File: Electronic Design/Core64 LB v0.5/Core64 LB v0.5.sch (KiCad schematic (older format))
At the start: 9 parts, among them J12 TEENSY Cur. Mon., J4 PRG, U2 Teensy3.2

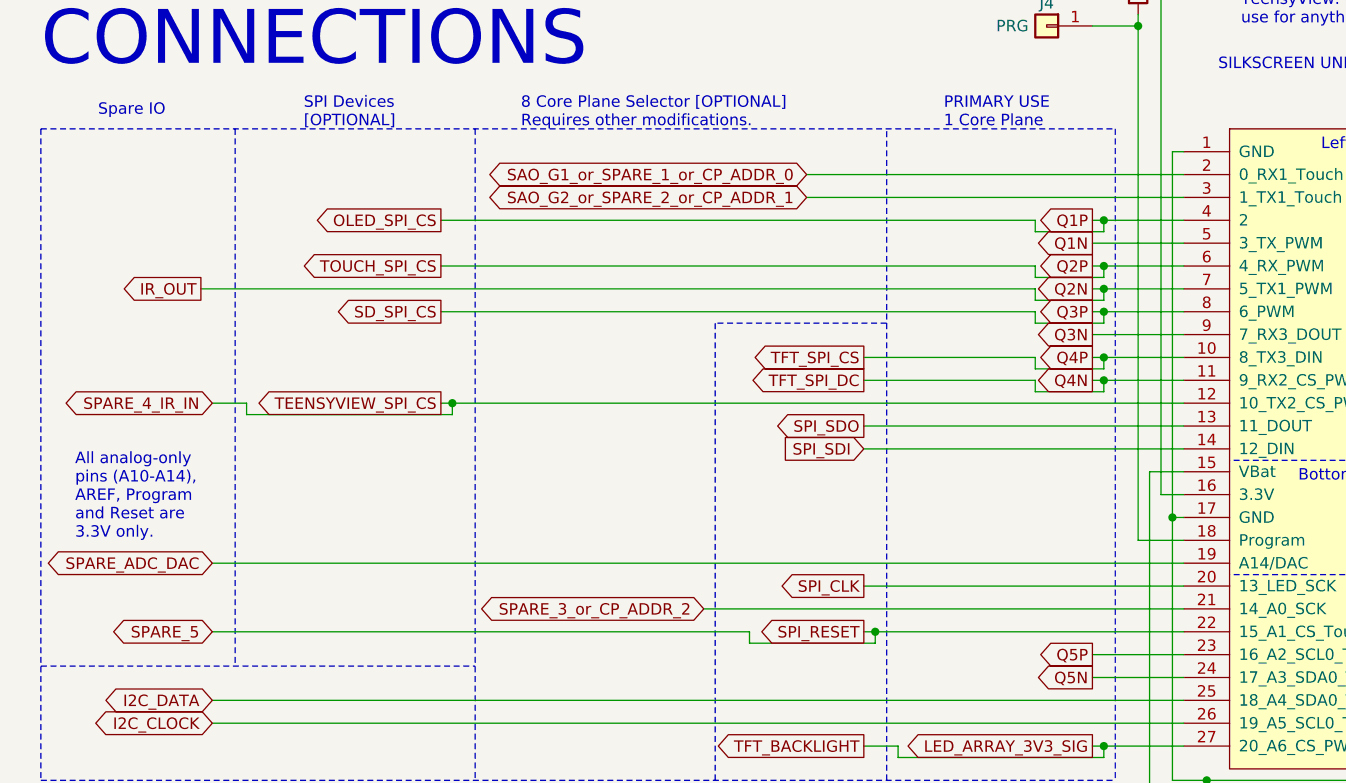
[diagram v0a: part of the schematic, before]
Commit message: LB Layout refinement for optional hall switches
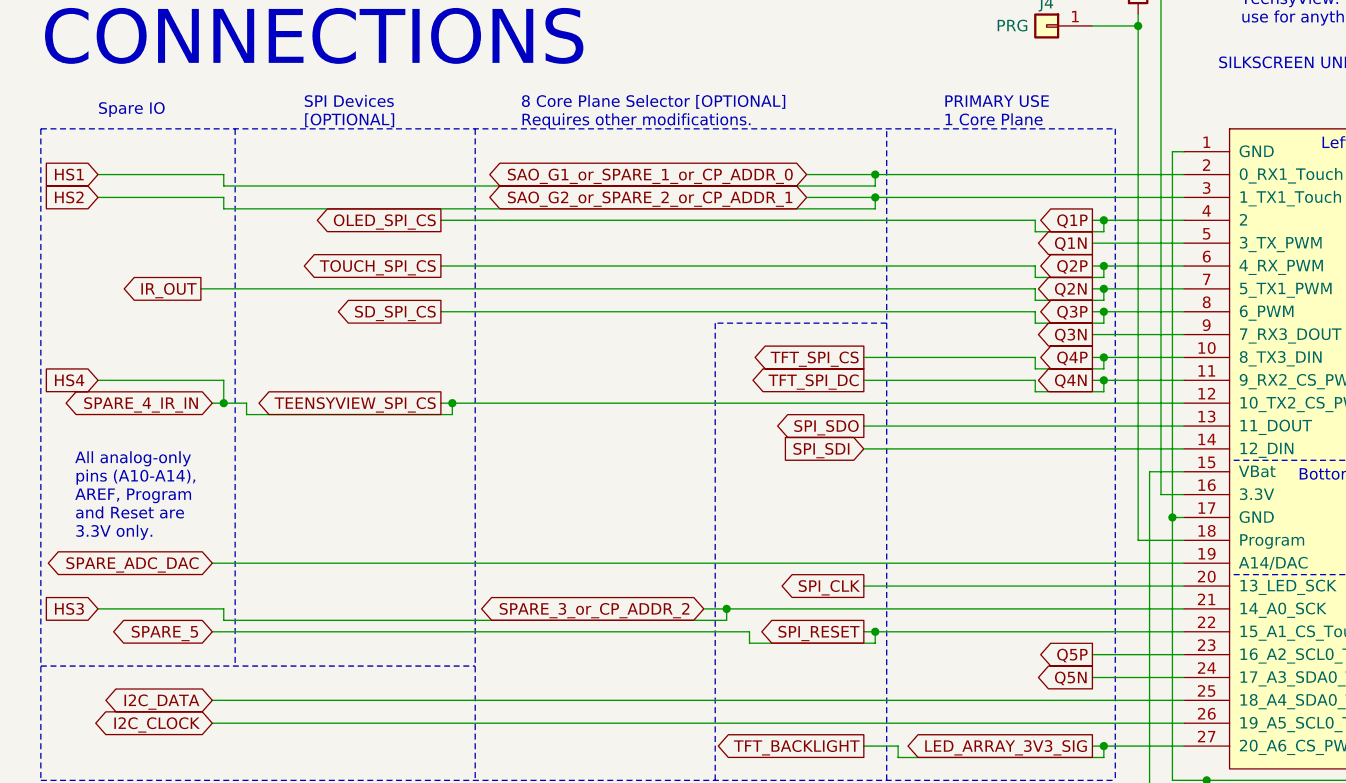
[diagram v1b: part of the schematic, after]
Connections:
- net SAO_G1_or_SPARE_1_or_CP_ADDR_0 renamed HS1
- net SAO_G2_or_SPARE_2_or_CP_ADDR_1 renamed HS2
- net SPARE_3_or_CP_ADDR_2 renamed HS3
- net SPARE_4_IR_IN renamed HS4
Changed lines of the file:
@@
 SPARE_4_IR_IN
 Wire Wire Line
-	3550 4750 5650 4750
+	3550 4750 3650 4750
 Wire Wire Line
 	4400 5400 4400 5350
 Wire Wire Line
-	5650 2850 4000 2850
-Wire Wire Line
-	5650 2950 4000 2950
+	5650 2850 4300 2850
+Wire Wire Line
+	5650 2950 4300 2950
 Wire Wire Line
 	7650 4150 8050 4150
@@
 Wire Wire Line
 	3750 4900 3750 4850
-Wire Wire Line
-	3750 4850 1400 4850
 Text GLabel 6450 1900 2    50   Output ~ 0
 TEENSY_3V3
@@
 	5300 3650 5300 3700
 Wire Wire Line
-	5000 3650 4250 3650
-Wire Wire Line
 	5300 3700 5000 3700
 Wire Wire Line
@@
 	1550 3900 1550 3850
 Wire Wire Line
-	1550 3850 1400 3850
+	1550 3850 1450 3850
 $Comp
 L Graphic:Logo_Open_Hardware_Small L4
@@
 F1 "Core64 LB v0.5 Driver.sch" 50
 $EndSheet
+Text GLabel 900  2850 0    50   Input ~ 0
+HS1
+Text GLabel 900  2950 0    50   Input ~ 0
+HS2
+Text GLabel 900  4750 0    50   Input ~ 0
+HS3
+Text GLabel 900  3750 0    50   Input ~ 0
+HS4
+Wire Wire Line
+	4300 2850 4300 2900
+Wire Wire Line
+	4300 2900 1450 2900
+Wire Wire Line
+	1450 2900 1450 2850
+Wire Wire Line
+	1450 2850 900  2850
+Connection ~ 4300 2850
+Wire Wire Line
+	4300 2850 4000 2850
+Wire Wire Line
+	900  2950 1450 2950
+Wire Wire Line
+	1450 2950 1450 3000
+Wire Wire Line
+	1450 3000 4300 3000
+Wire Wire Line
+	4300 3000 4300 2950
+Connection ~ 4300 2950
+Wire Wire Line
+	4300 2950 4000 2950
+Wire Wire Line
+	5000 3650 4250 3650
+Wire Wire Line
+	1450 3850 1450 3750
+Wire Wire Line
+	1450 3750 900  3750
+Connection ~ 1450 3850
+Wire Wire Line
+	1450 3850 1400 3850
+Wire Wire Line
+	3750 4850 1400 4850
+Wire Wire Line
+	3650 4750 3650 4800
+Wire Wire Line
+	3650 4800 1450 4800
+Wire Wire Line
+	1450 4800 1450 4750
+Wire Wire Line
+	1450 4750 900  4750
+Connection ~ 3650 4750
+Wire Wire Line
+	3650 4750 5650 4750
 $EndSCHEMATC

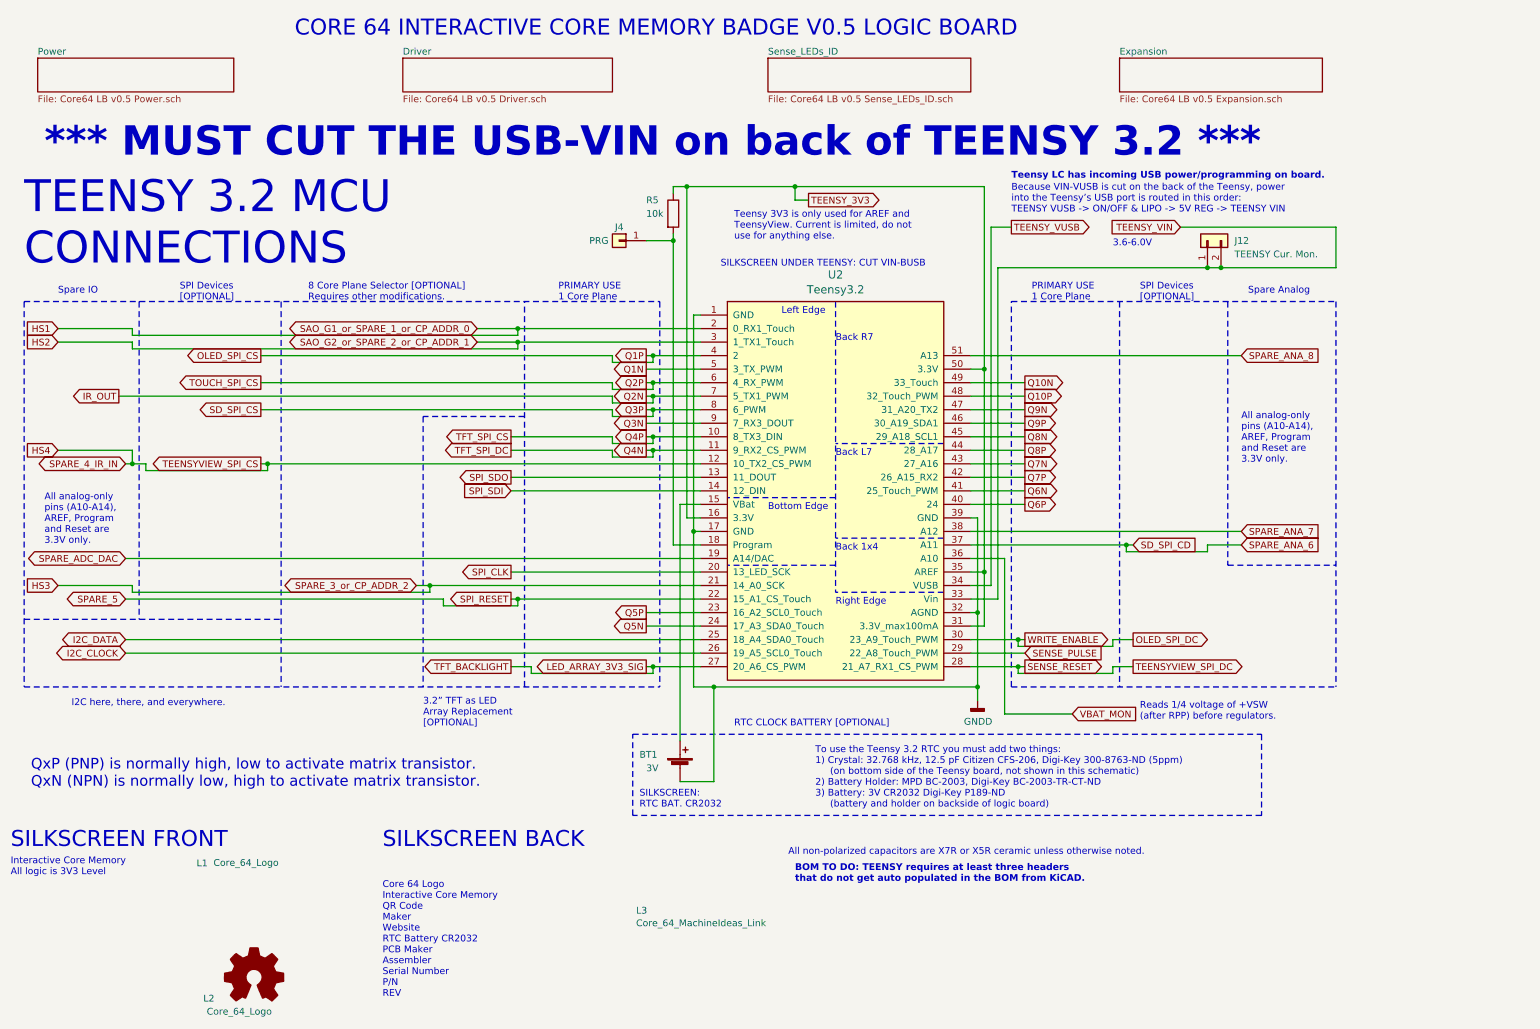
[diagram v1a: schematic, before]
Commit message: Connect row-col-0 to analog inputs for self-test mode
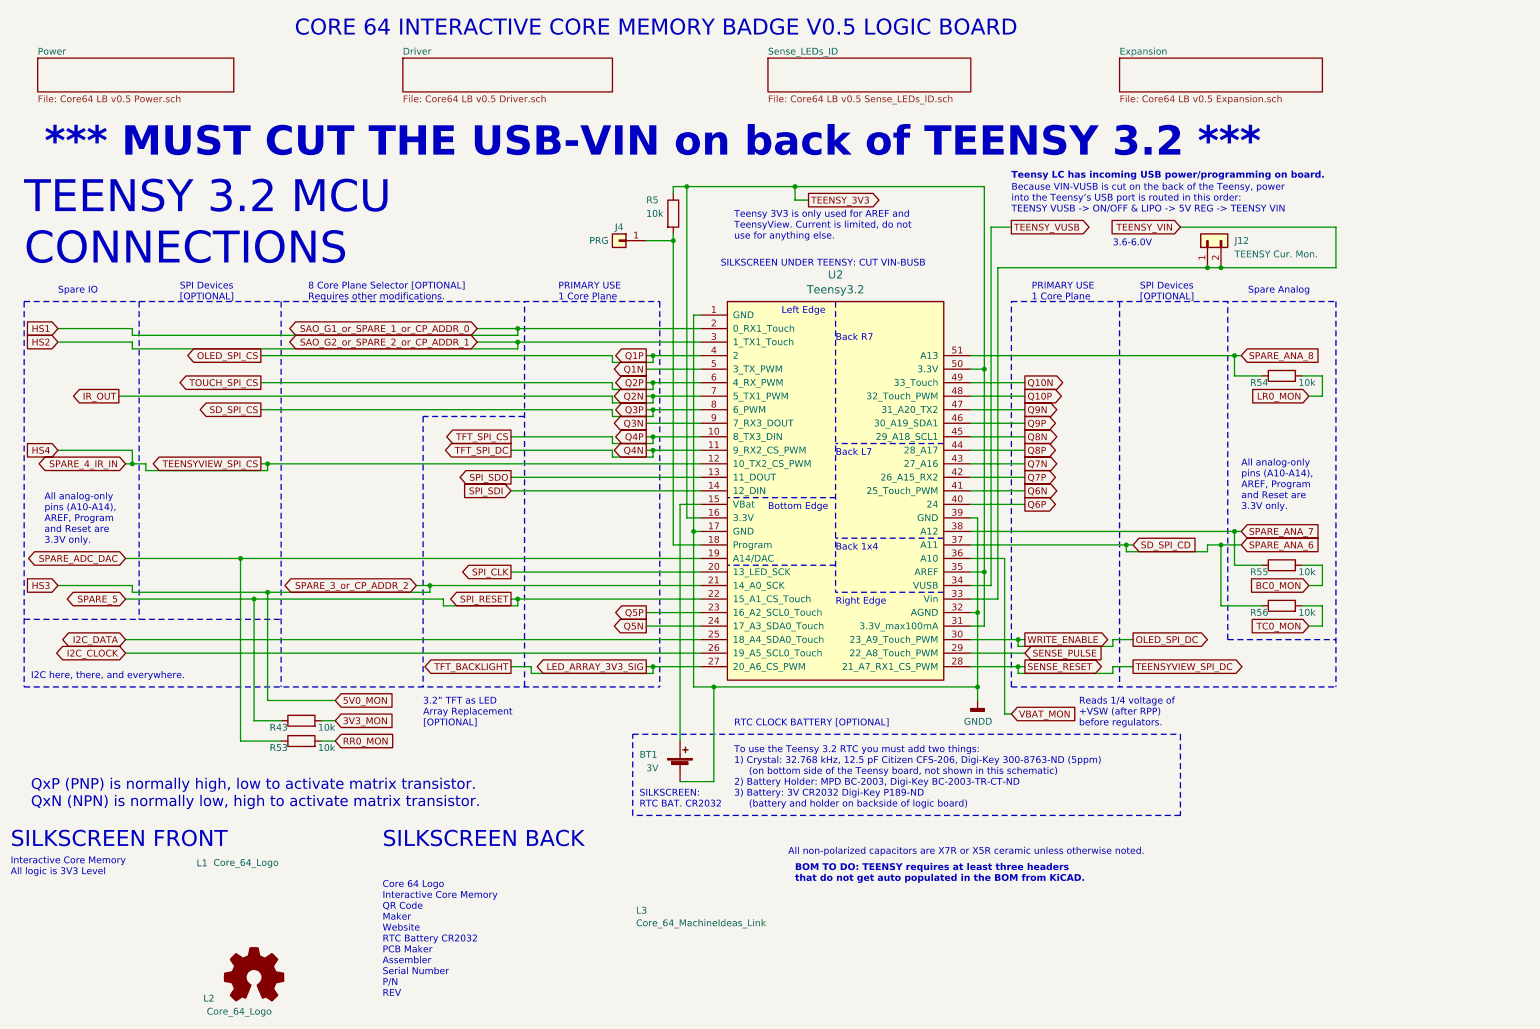
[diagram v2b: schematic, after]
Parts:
- added R43, R53, R54, R55, R56: 10k, Resistor_SMD:R_0805_2012Metric, symbol Device:R
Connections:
- net SD_SPI_CD: now also R56.1
- net SPARE_5: now also R43.1
- net SPARE_ADC_DAC: now also R53.1
- net SPARE_ANA_7: now also R55.1
- net SPARE_ANA_8: now also R54.1
- net HS3 renamed 5V0_MON
- new net 3V3_MON: R43.2
- new net BC0_MON: R55.2
- new net LR0_MON: R54.2
- new net RR0_MON: R53.2
- new net TC0_MON: R56.2
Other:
- note added: "Reads 1/4 voltage of\n+VSW (after RPP) \nbefore regulators."
- note removed: "Reads 1/4 voltage of +VSW\n(after RPP) before regulators."
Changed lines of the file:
@@
 Wire Wire Line
 	5250 3050 5300 3050
-Text Notes 8900 5750 0    50   ~ 0
-Reads 1/4 voltage of +VSW\n(after RPP) before regulators.
+Text Notes 8450 5800 0    50   ~ 0
+Reads 1/4 voltage of\n+VSW (after RPP) \nbefore regulators.
 Text Notes 7950 1750 0    50   ~ 10
 Teensy LC has incoming USB power/programming on board.
@@
 Wire Wire Line
 	7650 4550 7900 4550
-Text GLabel 8400 5700 2    50   Input ~ 0
+Text GLabel 7950 5700 2    50   Input ~ 0
 VBAT_MON
 Wire Wire Line
@@
 	7900 4550 7900 5700
 Wire Wire Line
-	7900 5700 8400 5700
+	7900 5700 7950 5700
 Connection ~ 7750 3150
 Wire Wire Line
@@
 	7650 3250 8050 3250
 Wire Wire Line
-	7650 3050 9650 3050
-Wire Wire Line
-	7650 4350 9650 4350
+	7650 3050 9600 3050
+Wire Wire Line
+	7650 4350 9600 4350
 Wire Wire Line
 	8850 4450 8800 4450
@@
 	5000 3050 2400 3050
 Wire Wire Line
-	5650 4550 1400 4550
+	5650 4550 2250 4550
 Text Notes 3300 6700 0    118  ~ 0
 SILKSCREEN BACK
@@
 Wire Wire Line
 	5450 2200 5450 2150
-Text Notes 6500 6400 0    50   ~ 0
+Text Notes 5900 6400 0    50   ~ 0
 To use the Teensy 3.2 RTC you must add two things:\n1) Crystal: 32.768 kHz, 12.5 pF Citizen CFS-206, Digi-Key 300-8763-ND (5ppm)\n     (on bottom side of the Teensy board, not shown in this schematic)\n2) Battery Holder: MPD BC-2003, Digi-Key BC-2003-TR-CT-ND\n3) Battery: 3V CR2032 Digi-Key P189-ND\n     (battery and holder on backside of logic board)\n
 Connection ~ 7700 5500
@@
 	9500 2400 10350 2400
 Wire Notes Line
-	9550 2650 9550 4600
-Wire Notes Line
 	10350 2650 10350 5500
 Text Notes 9700 2600 0    50   ~ 0
@@
 	5750 5500 7700 5500
 Wire Notes Line
-	5150 5850 9800 5850
-Wire Notes Line
-	9800 5850 9800 6450
-Wire Notes Line
-	9800 6450 5150 6450
-Wire Notes Line
 	5150 6450 5150 5850
 Text Notes 5900 5800 0    50   ~ 0
@@
 Wire Notes Line
 	650  5000 2550 5000
-Text Notes 1000 5650 0    50   ~ 0
+Text Notes 700  5450 0    50   ~ 0
 I2C here, there, and everywhere.
 Wire Notes Line
@@
 	9400 4500 9400 4450
 Wire Wire Line
-	9400 4450 9650 4450
+	9400 4450 9500 4450
 Connection ~ 8800 4450
 Wire Wire Line
 	8800 4450 7650 4450
-Text Notes 700  6250 0    79   ~ 0
+Text Notes 700  6400 0    79   ~ 0
 QxP (PNP) is normally high, low to activate matrix transistor.\nQxN (NPN) is normally low, high to activate matrix transistor.
 Text Notes 8700 2250 0    50   ~ 0
 3.6-6.0V
-Text Notes 9650 3850 0    50   ~ 0
+Text Notes 9650 4200 0    50   ~ 0
 All analog-only\npins (A10-A14),\nAREF, Program\nand Reset are\n3.3V only.
 Text Notes 800  4450 0    50   ~ 0
@@
 Wire Wire Line
 	8000 5150 8050 5150
-Wire Notes Line
-	9550 4600 10350 4600
 Wire Wire Line
 	5250 3150 5650 3150
@@
 	1450 3850 1400 3850
 Wire Wire Line
-	3750 4850 1400 4850
+	3750 4850 2350 4850
 Wire Wire Line
 	3650 4750 3650 4800
 Wire Wire Line
-	3650 4800 1450 4800
+	3650 4800 2450 4800
 Wire Wire Line
 	1450 4800 1450 4750
@@
 Wire Wire Line
 	3650 4750 5650 4750
+Text GLabel 2950 5600 2    50   Input ~ 0
+5V0_MON
+Text GLabel 2950 5750 2    50   Input ~ 0
+3V3_MON
+Wire Wire Line
+	2450 4800 2450 5600
+Connection ~ 2450 4800
+Wire Wire Line
+	2450 4800 1450 4800
+Wire Wire Line
+	2350 4850 2350 5750
+Wire Wire Line
+	2350 5750 2550 5750
+Connection ~ 2350 4850
+Wire Wire Line
+	2350 4850 1400 4850
+Text GLabel 10150 5050 0    50   Input ~ 0
+TC0_MON
+Text GLabel 10150 4750 0    50   Input ~ 0
+BC0_MON
+Wire Notes Line
+	9550 5150 10350 5150
+Wire Notes Line
+	9550 5150 9550 2650
+Wire Wire Line
+	9600 4350 9600 4600
+Wire Wire Line
+	9600 4600 9800 4600
+Connection ~ 9600 4350
+Wire Wire Line
+	9600 4350 9650 4350
+Wire Wire Line
+	9500 4450 9500 4900
+Connection ~ 9500 4450
+Wire Wire Line
+	9500 4450 9650 4450
+Text GLabel 10150 3350 0    50   Input ~ 0
+LR0_MON
+Wire Wire Line
+	9600 3050 9600 3200
+Connection ~ 9600 3050
+Wire Wire Line
+	9600 3050 9650 3050
+Text GLabel 2950 5900 2    50   Input ~ 0
+RR0_MON
+Wire Wire Line
+	2550 5900 2250 5900
+Wire Wire Line
+	2250 5900 2250 4550
+Connection ~ 2250 4550
+Wire Wire Line
+	2250 4550 1400 4550
+$Comp
+L Device:R R?
+U 1 1 60646D8E
+P 2700 5750
+AR Path="/5E755787/60646D8E" Ref="R?"  Part="1"
+AR Path="/5E755AC8/5D2551FF/60646D8E" Ref="R?"  Part="1"
+AR Path="/60646D8E" Ref="R43"  Part="1"
+F 0 "R43" V 2650 5850 50  0000 L CNN
+F 1 "10k" V 2650 5500 50  0000 L CNN
+F 2 "Resistor_SMD:R_0805_2012Metric" V 2630 5750 50  0001 C CNN
+F 3 "~" H 2700 5750 50  0001 C CNN
+	1    2700 5750
+	0    -1   -1   0
+$EndComp
+$Comp
+L Device:R R?
+U 1 1 60648F4B
+P 2700 5900
+AR Path="/5E755787/60648F4B" Ref="R?"  Part="1"
+AR Path="/5E755AC8/5D2551FF/60648F4B" Ref="R?"  Part="1"
+AR Path="/60648F4B" Ref="R53"  Part="1"
+F 0 "R53" V 2650 6000 50  0000 L CNN
+F 1 "10k" V 2650 5650 50  0000 L CNN
+F 2 "Resistor_SMD:R_0805_2012Metric" V 2630 5900 50  0001 C CNN
+F 3 "~" H 2700 5900 50  0001 C CNN
+	1    2700 5900
+	0    -1   -1   0
+$EndComp
+Wire Wire Line
+	2850 5900 2950 5900
+Wire Wire Line
+	2850 5750 2950 5750
+Wire Wire Line
+	2450 5600 2950 5600
+$Comp
+L Device:R R?
+U 1 1 60683EFC
+P 9950 4600
+AR Path="/5E755787/60683EFC" Ref="R?"  Part="1"
+AR Path="/5E755AC8/5D2551FF/60683EFC" Ref="R?"  Part="1"
+AR Path="/60683EFC" Ref="R55"  Part="1"
+F 0 "R55" V 9900 4700 50  0000 L CNN
+F 1 "10k" V 9900 4350 50  0000 L CNN
+F 2 "Resistor_SMD:R_0805_2012Metric" V 9880 4600 50  0001 C CNN
+F 3 "~" H 9950 4600 50  0001 C CNN
+	1    9950 4600
+	0    -1   -1   0
+$EndComp
+Wire Notes Line
+	9200 5850 9200 6450
+Wire Notes Line
+	5150 5850 9200 5850
+Wire Notes Line
+	9200 6450 5150 6450
+$Comp
+L Device:R R?
+U 1 1 606B32F6
+P 9950 3200
+AR Path="/5E755787/606B32F6" Ref="R?"  Part="1"
+AR Path="/5E755AC8/5D2551FF/606B32F6" Ref="R?"  Part="1"
+AR Path="/606B32F6" Ref="R54"  Part="1"
+F 0 "R54" V 9900 3300 50  0000 L CNN
+F 1 "10k" V 9900 2950 50  0000 L CNN
+F 2 "Resistor_SMD:R_0805_2012Metric" V 9880 3200 50  0001 C CNN
+F 3 "~" H 9950 3200 50  0001 C CNN
+	1    9950 3200
+	0    -1   -1   0
+$EndComp
+Wire Wire Line
+	10100 3200 10250 3200
+Wire Wire Line
+	10250 3200 10250 3350
+Wire Wire Line
+	10250 3350 10150 3350
+Wire Wire Line
+	9600 3200 9800 3200
+Wire Wire Line
+	10100 4600 10250 4600
+Wire Wire Line
+	10250 4600 10250 4750
+Wire Wire Line
+	10250 4750 10150 4750
+$Comp
+L Device:R R?
+U 1 1 606EF222
+P 9950 4900
+AR Path="/5E755787/606EF222" Ref="R?"  Part="1"
+AR Path="/5E755AC8/5D2551FF/606EF222" Ref="R?"  Part="1"
+AR Path="/606EF222" Ref="R56"  Part="1"
+F 0 "R56" V 9900 5000 50  0000 L CNN
+F 1 "10k" V 9900 4650 50  0000 L CNN
+F 2 "Resistor_SMD:R_0805_2012Metric" V 9880 4900 50  0001 C CNN
+F 3 "~" H 9950 4900 50  0001 C CNN
+	1    9950 4900
+	0    -1   -1   0
+$EndComp
+Wire Wire Line
+	9500 4900 9800 4900
+Wire Wire Line
+	10100 4900 10250 4900
+Wire Wire Line
+	10250 4900 10250 5050
+Wire Wire Line
+	10250 5050 10150 5050
 $EndSCHEMATC

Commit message: LB layout redlines
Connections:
- net VBAT_MON renamed BAT_MON
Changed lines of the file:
@@
 	7650 4550 7900 4550
 Text GLabel 7950 5700 2    50   Input ~ 0
-VBAT_MON
+BAT_MON
 Wire Wire Line
 	7650 4750 7800 4750
